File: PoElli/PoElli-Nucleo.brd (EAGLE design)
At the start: 57.5 x 70 mm, 107 parts, among them J3 M022.54MM, J4 M022.54MM, Q3 FDMC2674HANDSOLDERING, Q4 FDMC2674HANDSOLDERING, T1 Coilcraft 230NL, T2 FLYBACK-3_OUTPUTS_749119350, U4 LT3748, U5 TPS2378, U6 ENC424J600, X1 POE-TP-SHIELDED-LEDSTE1888250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

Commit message: Fix SPI pin order
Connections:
- net ETH_MOSI: now also U$2.CN10_29; no longer U$2.CN10_25
- net ETH_SCK: now also U$2.CN10_31; no longer U$2.CN10_29
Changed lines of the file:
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@@
 <contactref element="U6" pad="37"/>
 <contactref element="TP3" pad="P$1"/>
-<contactref element="U$2" pad="CN10_29"/>
-<wire x1="56.7" y1="76.59" x2="96.36" y2="84.02" width="0" layer="19" extent="1-1"/>
+<contactref element="U$2" pad="CN10_31"/>
+<wire x1="56.7" y1="76.59" x2="98.9" y2="84.02" width="0" layer="19" extent="1-1"/>
 <wire x1="24.13" y1="62.8" x2="56.7" y2="76.59" width="0" layer="19" extent="1-1"/>
 </signal>
@@
 <contactref element="U6" pad="36"/>
 <contactref element="TP4" pad="P$1"/>
-<contactref element="U$2" pad="CN10_25"/>
-<wire x1="56.7" y1="77.39" x2="91.28" y2="84.02" width="0" layer="19" extent="1-1"/>
+<contactref element="U$2" pad="CN10_29"/>
+<wire x1="56.7" y1="77.39" x2="96.36" y2="84.02" width="0" layer="19" extent="1-1"/>
 <wire x1="32.55" y1="58.3" x2="56.7" y2="77.39" width="0" layer="19" extent="1-1"/>
 </signal>

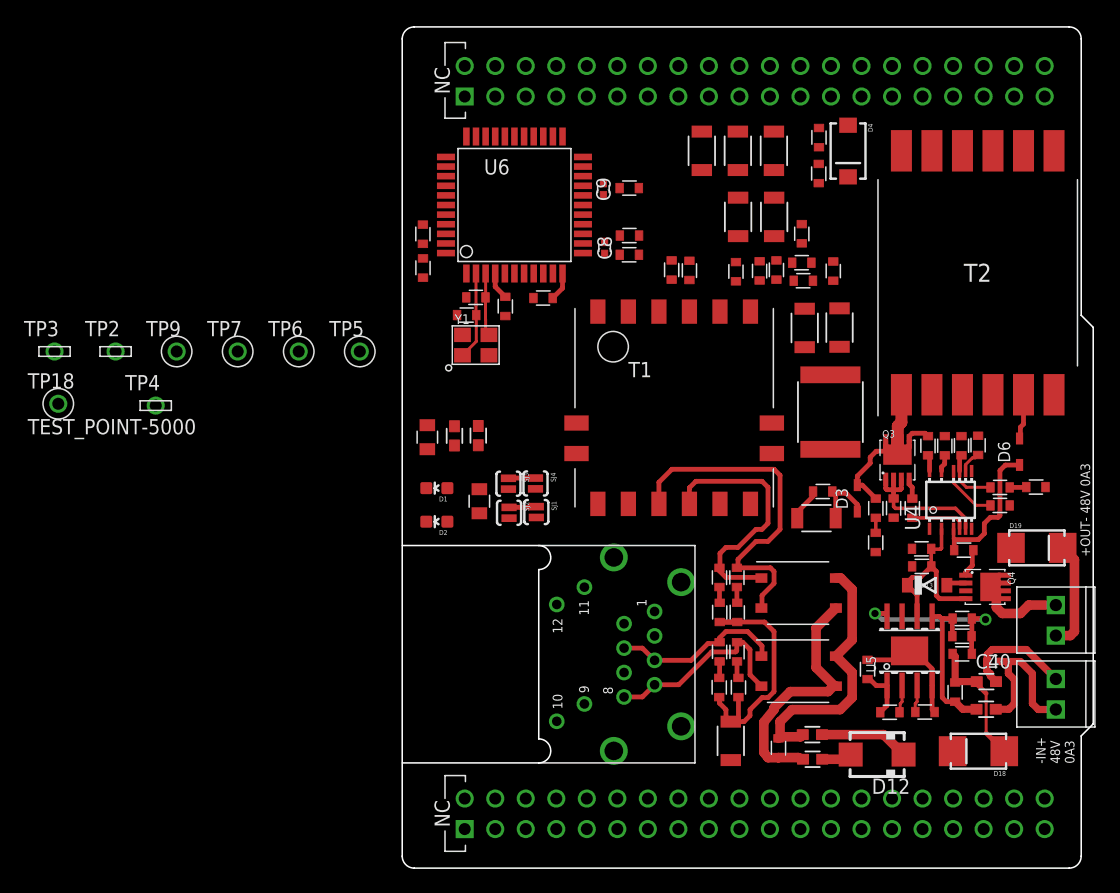
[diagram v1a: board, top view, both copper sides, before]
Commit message: Component placement complete
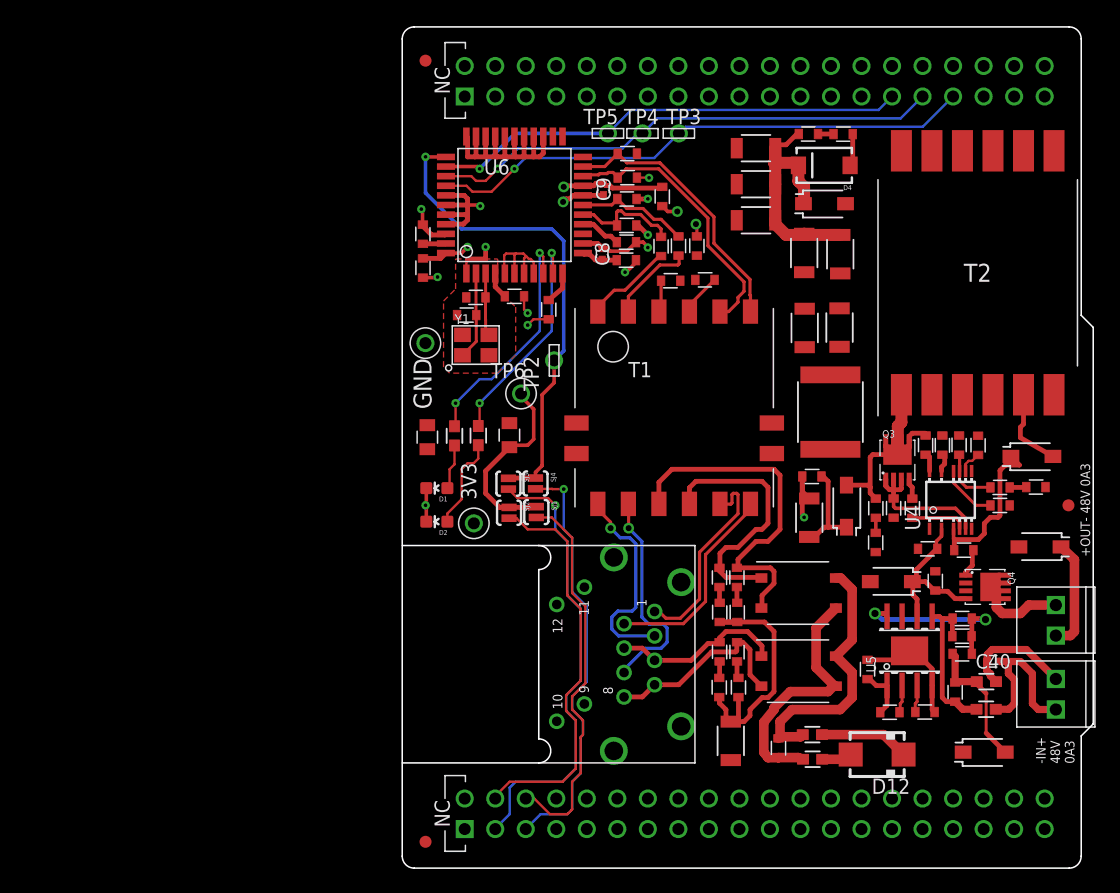
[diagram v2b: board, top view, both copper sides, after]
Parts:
- removed TP18: TEST_POINT-5000, ELL-i-Passives:TP_5000
- removed TP7: (no value), ELL-i-Passives:TP_5000
- added 3V3: (no value), ELL-i-Passives:TP_5000
- added D10: MMSZ4694, ELL-i-DIscreteSemi:SOD-123FL-A
- added FID1, FID2, FID3: FIDUCIAL1X2, SparkFun-Aesthetics:FIDUCIAL-1X2
- D13: value 18V -> MMSZ4694 (8V2); device ELL-i-DIscreteSemi:SOD-123FL -> ELL-i-DIscreteSemi:SOD-123FL-A
- D18, D19: value B2100 -> SMD1200PL; device ELL-i-DIscreteSemi:DIODE-B2100 -> ELL-i-DIscreteSemi:SOD-123FL-A
- D3: value BAV20WS -> SMD1200PL; device ELL-i-DIscreteSemi:SOD-323 -> ELL-i-DIscreteSemi:SOD-123FL-A
- D6: value BAS70J -> SMD1200PL; device ELL-i-DIscreteSemi:SOD-323 -> ELL-i-DIscreteSemi:SOD-123FL-A
- TP5: value (none) -> TEST_POINT-5021; device ELL-i-Passives:TP_5000 -> ELL-i-Passives:TP_5021
- moved TP3 55.0 mm to (76.1, 81.0)
- moved TP4 46.4 mm to (73.0, 81.0)
- moved TP2 36.5 mm to (65.7, 62.1), turned to 90 degrees
- moved TP5 27.5 mm to (70.2, 81.0)
- moved TP9 20.7 mm to (55.0, 63.5)
- moved TP6 18.8 mm to (63.0, 59.3)
- moved R13 18.8 mm to (71.8, 77.3), turned to 0 degrees
- moved R8 15.5 mm to (71.8, 75.5)
- moved R9 15.4 mm to (71.7, 73.3)
- moved R12 13.4 mm to (71.8, 79.3), turned to 0 degrees
- moved C12 11.6 mm to (75.4, 68.7), turned to 180 degrees
- moved C15 8.45 mm to (74.6, 71.5), turned to 90 degrees
- moved C11 8.39 mm to (76.0, 71.6)
- moved C46 6.31 mm to (89.5, 70.9)
- moved C47 6.26 mm to (86.5, 71.0)
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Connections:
- removed net N$36: D1.A, R4.P$2
- removed net N$38: D2.A, R3.P$1
- new net LEDA: D2.A, R3.P$1, X1.10
- new net LEDB: D1.A, R4.P$2, X1.11
- net +3V3: now also 3V3.P$1; no longer TP7.P$1
- net GNDA: now also D10.A, X1.12, X1.9
- net SGND: no longer TP18.P$1
- net VIN: now also D10.C
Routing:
- net GNDA: track 0.00 -> 76.4 mm, vias 0 -> 10
- net ETH_SCK: track 0.00 -> 45.7 mm, vias 0 -> 1
- net ETH_MOSI: track 0.00 -> 42.7 mm, vias 0 -> 1
- net ETH_MISO: track 0.00 -> 39.7 mm, vias 0 -> 1
- net ETH_SS: track 2.27 -> 40.8 mm, vias 0 -> 1
- net N$11: track 0.00 -> 38.2 mm, vias 0 -> 1
- net N$12: track 0.00 -> 35.6 mm, vias 0 -> 1
- net N$13: track 0.00 -> 33.7 mm
- net N$14: track 0.00 -> 32.5 mm
- net TPOUT+: track 0.00 -> 23.0 mm
- net TPOUT-: track 0.00 -> 22.7 mm
- net VIN: track 0.00 -> 21.4 mm
- net N$41: track 0.00 -> 19.8 mm, vias 0 -> 2
- net N$42: track 0.00 -> 18.7 mm, vias 0 -> 2
- net RX-: track 0.00 -> 18.3 mm, vias 0 -> 1
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- added copper zone on layer 15, net ENC-3V3
- added copper zone on layer 1, net GNDA
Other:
- board text added: "GND"

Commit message: component placement, planes final.
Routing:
- net +3V3: track 2.41 -> 113.2 mm, vias 2 -> 5
- net GNDA: track 76.4 -> 129.4 mm, vias 10 -> 27
- net RTN: track 15.4 -> 60.8 mm, vias 0 -> 17
- net N$11: track 38.2 -> 0.00 mm, vias 1 -> 0
- net VDD: track 17.4 -> 54.5 mm, vias 1 -> 12
- net N$12: track 35.6 -> 0.00 mm, vias 1 -> 0
- net N$13: track 33.7 -> 0.00 mm
- net N$14: track 32.5 -> 0.00 mm
- net ETH_INT: track 16.0 -> 44.9 mm, vias 0 -> 2
- net SGND: track 0.00 -> 24.9 mm
- net TRAFO_OUT: track 2.69 -> 25.4 mm
- net ENC-3V3: track 18.7 -> 40.0 mm, vias 3 -> 8
- net TPINCT: track 5.12 -> 16.1 mm
- net VIN: track 21.4 -> 32.0 mm, vias 0 -> 2
- net VSS: track 12.5 -> 7.65 mm, vias 0 -> 3
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- added copper zone on layer 2, net GNDA
- added copper zone on layer 2, net RTN
- added copper zone on layer 15, net VDD
- added copper zone on layer 15, net VIN
- added copper zone on layer 1, net VSS
- added copper zone on layer 2, net VSS

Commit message: Layout complete, except silkscreen.
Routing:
- net N$11: track 0.00 -> 36.6 mm
- net N$13: track 0.00 -> 33.2 mm, vias 0 -> 1
- net N$12: track 0.00 -> 33.0 mm, vias 0 -> 1
- net N$14: track 0.00 -> 30.5 mm, vias 0 -> 1
- net LEDA: track 7.43 -> 32.6 mm
- net LEDB: track 3.80 -> 23.8 mm, vias 0 -> 1
- net RTN: vias 17 -> 18
- added copper zone on layer 15, net RTN

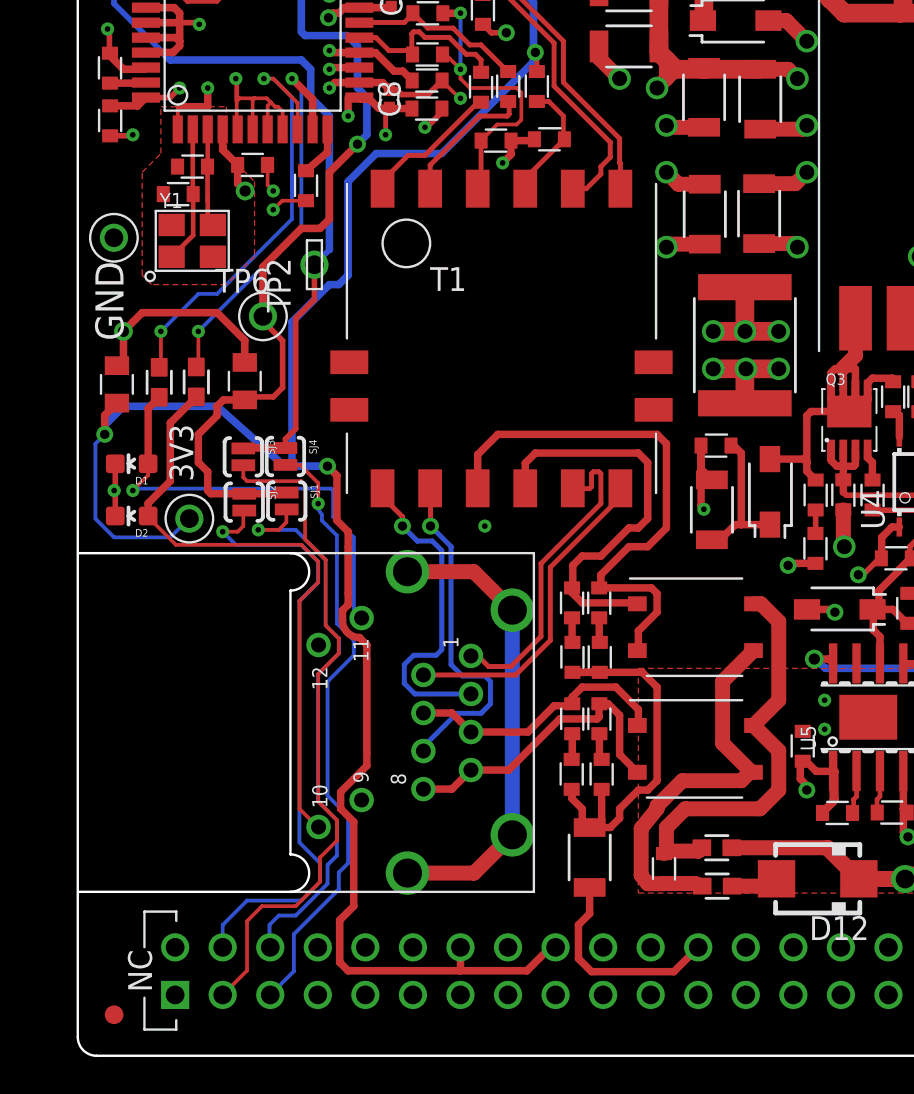
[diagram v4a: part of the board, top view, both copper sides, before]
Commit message: Copper layers, complete, DRC ok. Silkscreen has to be adjusted.
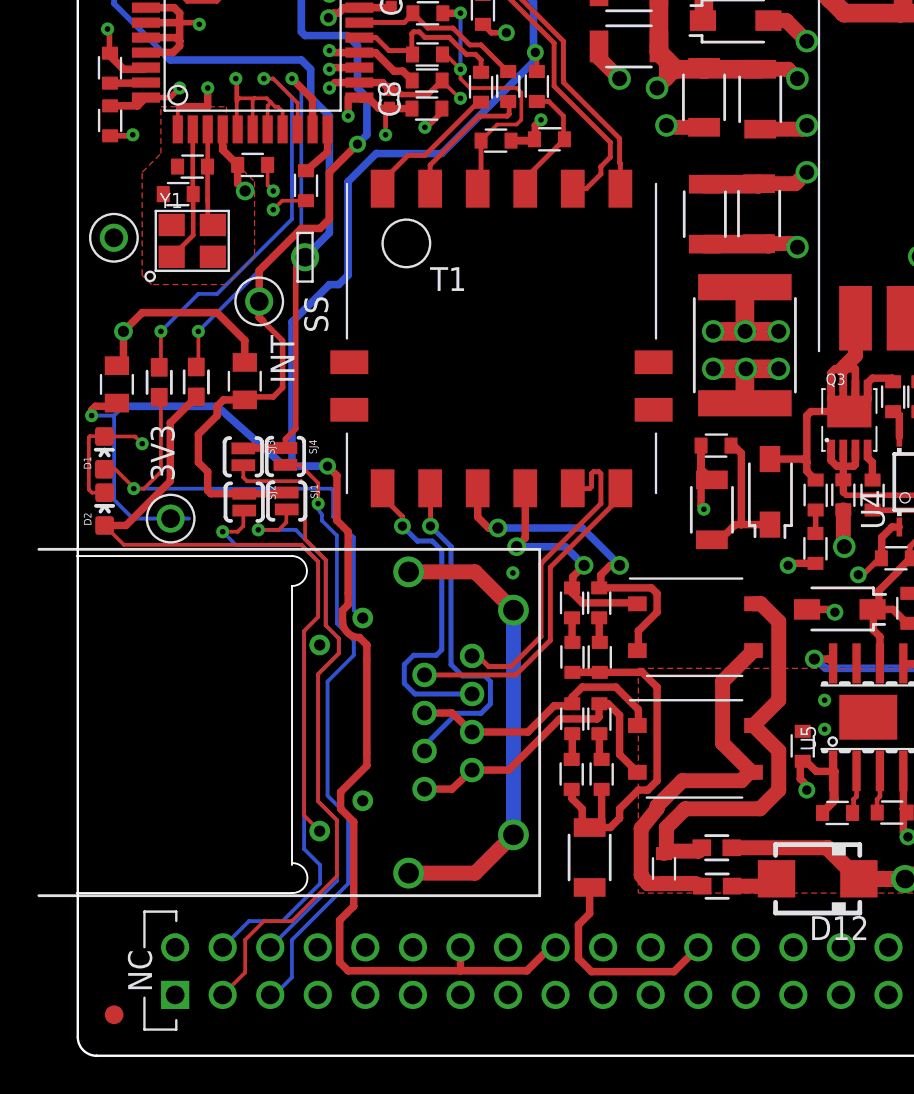
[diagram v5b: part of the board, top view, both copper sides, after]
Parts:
- removed TP2: (no value), ELL-i-Passives:TP_5021
- removed TP6: (no value), ELL-i-Passives:TP_5000
- added INT: (no value), ELL-i-Passives:TP_5000
- added SS: (no value), ELL-i-Passives:TP_5021
- X1: value POE-TP-SHIELDED-LEDSTE1888250 -> POE-TP-SHIELDED-LEDSTE1888250-A; device ELL-i-Connectors:TE1888250 -> ELL-i-Connectors:TE1888250-A
- moved X1 11.4 mm to (64.5, 37.6)
- moved D1 1.57 mm to (54.5, 52.0), turned to 0 degrees
- moved D2 1.50 mm to (54.5, 49.0), turned to 0 degrees
- moved 3V3 1.00 mm to (58.0, 48.5)
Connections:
- net ETH_INT: now also INT.P$1; no longer TP6.P$1
- net ETH_SS: now also SS.P$1; no longer TP2.P$1
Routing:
- net POE_A-: track 29.0 -> 18.8 mm, vias 0 -> 2
- net POE_A+: track 21.6 -> 12.8 mm, vias 0 -> 2
- net GNDA: track 129.4 -> 134.9 mm, vias 27 -> 26
- net LEDA: track 32.6 -> 37.1 mm
- net LEDB: track 23.8 -> 26.1 mm
- net RTN: track 60.8 -> 62.2 mm, vias 18 -> 17
- net +3V3: track 113.2 -> 111.9 mm
- net N$13: track 33.2 -> 32.3 mm
- net SGND: track 24.9 -> 25.4 mm
- net N$14: track 30.5 -> 30.0 mm
- added copper zone on layer 2, net N$1
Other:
- board text removed: "GND"

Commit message: Silkscreen ok
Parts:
- removed TP5: TEST_POINT-5021, ELL-i-Passives:TP_5021
- added MISO: MISO, ELL-i-Passives:TP_5021
- 3V3: value (none) -> 3V3
- C40: device ELL-i-Passives:SMD0402-B -> ELL-i-Passives:SMD0603-B
- D1: value GREEN -> LINK
- D2: value GREEN -> ACT
- INT: value (none) -> TEST_POINT-5000
- SS: value (none) -> SS
- TP3: value (none) -> SCK
- TP4: value (none) -> MOSI
- TP9: value (none) -> GND
- moved TP3 1.80 mm to (77.9, 81.0)
- moved TP4 1.80 mm to (74.8, 81.0)
- moved C40 0.79 mm to (102.5, 37.8), turned to 270 degrees
- moved C33 0.46 mm to (92.0, 49.7)
- moved Q3 0.40 mm to (93.9, 53.8)
- moved R22 0.35 mm to (96.8, 46.0)
- moved U4 0.30 mm to (98.7, 50.1)
- moved C30 0.25 mm to (99.8, 46.0)
- moved C35 0.20 mm to (91.6, 36.3)
- moved D13 0.10 mm to (93.8, 43.8)
- moved R23 0.10 mm to (93.6, 32.7)
- moved R26 0.10 mm to (97.4, 43.8)
- moved R28 0.10 mm to (95.5, 49.7)
- moved R32 0.10 mm to (94.0, 49.7)
- moved R27 0.10 mm to (92.5, 46.8)
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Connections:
- net ETH_MISO: now also MISO.P$1; no longer TP5.P$1
- net N$53: now also C40.P$1; no longer C40.1
- net N$55: now also C40.P$2; no longer C40.2
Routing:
- net RTN: track 62.2 -> 60.3 mm
- net N$28: track 21.3 -> 22.9 mm, vias 0 -> 4
- net N$10: track 15.9 -> 17.5 mm, vias 0 -> 4
- net N$53: track 9.52 -> 10.5 mm
- net +3V3: track 111.9 -> 110.9 mm
- net VSS: track 7.65 -> 7.73 mm, vias 3 -> 9
- added copper zone on layer 16, net N$10
- added copper zone on layer 16, net N$28
- added copper zone on layer 16, net VSS
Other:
- board text added: "AC"
- board text added: "DC"

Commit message: PoELLi 1.0
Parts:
- added LOGO1: OSHW-LOGOM, SparkFun-Aesthetics:OSHW-LOGO-M
- SJ1, SJ3: value SOLDERJUMPERNO -> SOLDERJUMPERNC2; device SparkFun-Passives:SJ_2S-NO -> SparkFun-Passives:SJ_2S-NOTRACE
- moved TP3 9.15 mm to (68.7, 81.0)
- moved MISO 6.50 mm to (75.2, 81.0)
- moved TP4 3.50 mm to (78.3, 81.0)
- moved D19 1.41 mm to (105.1, 47.6)
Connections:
- removed net N$10: J3.P2, Q4.5, Q4.6, Q4.7, Q4.8, Q4.F1
- removed net N$21: D19.C, J3.P1
- new net N$3: J3.P1, Q4.5, Q4.6, Q4.7, Q4.8, Q4.F1
- new net N$4: D19.C, J3.P2
- net ETH_MISO: now also U$2.CN10_13; no longer U$2.CN10_27
- net ETH_MOSI: now also U$2.CN10_15; no longer U$2.CN10_29
- net ETH_SCK: now also U$2.CN10_11; no longer U$2.CN10_31
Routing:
- net ETH_SCK: track 45.7 -> 20.5 mm
- net N$3: track 0.00 -> 19.6 mm, vias 0 -> 4
- net N$10: track 17.5 -> 0.00 mm, vias 4 -> 0
- net ETH_MISO: track 39.7 -> 25.0 mm
- net ETH_MOSI: track 42.8 -> 28.3 mm
- net N$21: track 9.25 -> 0.00 mm
- net N$4: track 0.00 -> 6.13 mm
- net VDD: track 54.4 -> 51.4 mm, vias 12 -> 11
- net VSS: track 7.73 -> 9.95 mm, vias 9 -> 10
- net GNDA: track 134.9 -> 133.8 mm, vias 26 -> 27
- added copper zone on layer 16, net N$3
- removed copper zone on layer 16, net N$10
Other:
- board text added: "48V 0A3 -IN+"
- board text added: "48V 0A3 -OUT+"
- board text added: "ELL-i"
- board text added: "OPEN HARDWARE"
- board text added: "Open source co-operative"
- board text added: "PoELLi-Nucleo 1.0"
- board text added: "QC pass"
- board text added: "http://ell-i.org/"
- board text added: "https://github.com/Ell-i /ELL-i-Eagle-Boards"
- board text removed: "+OUT- 48V 0A3"
- board text removed: "-IN+ 48V 0A3"

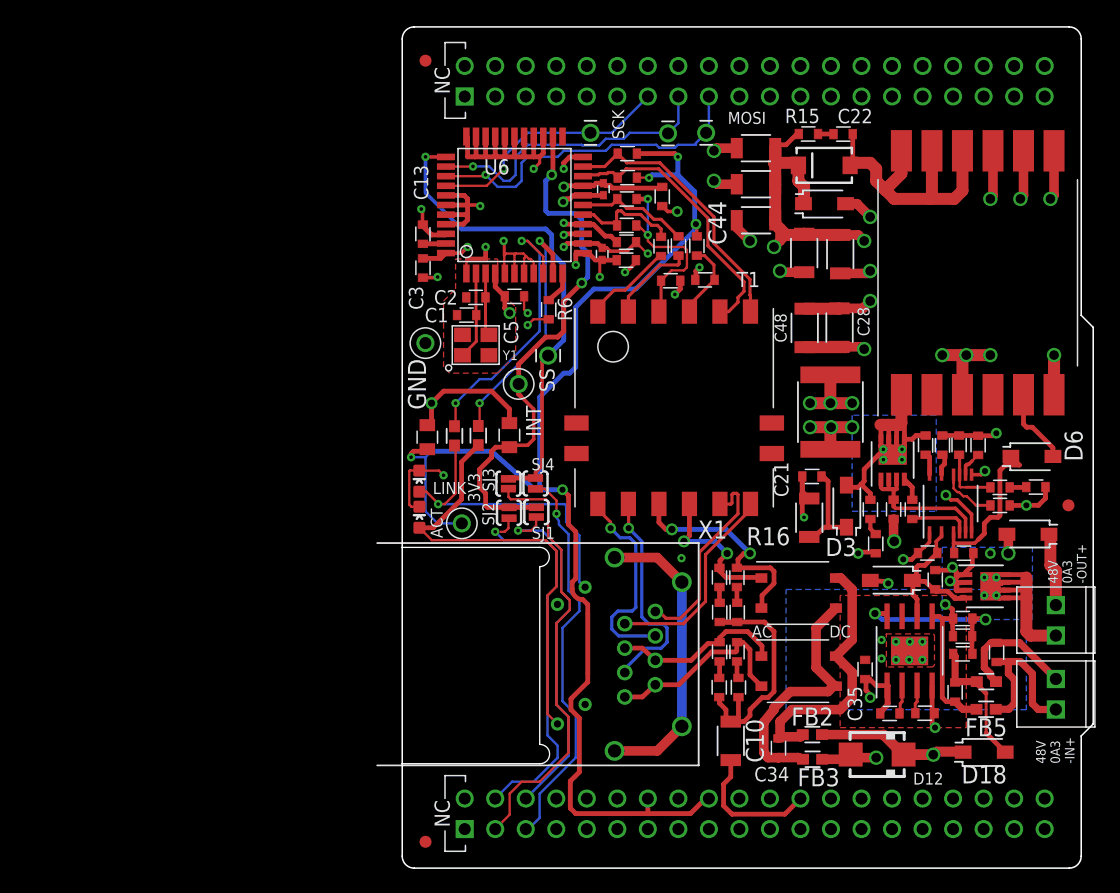
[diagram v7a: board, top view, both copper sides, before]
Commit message: Fix Bridge rectifier connection
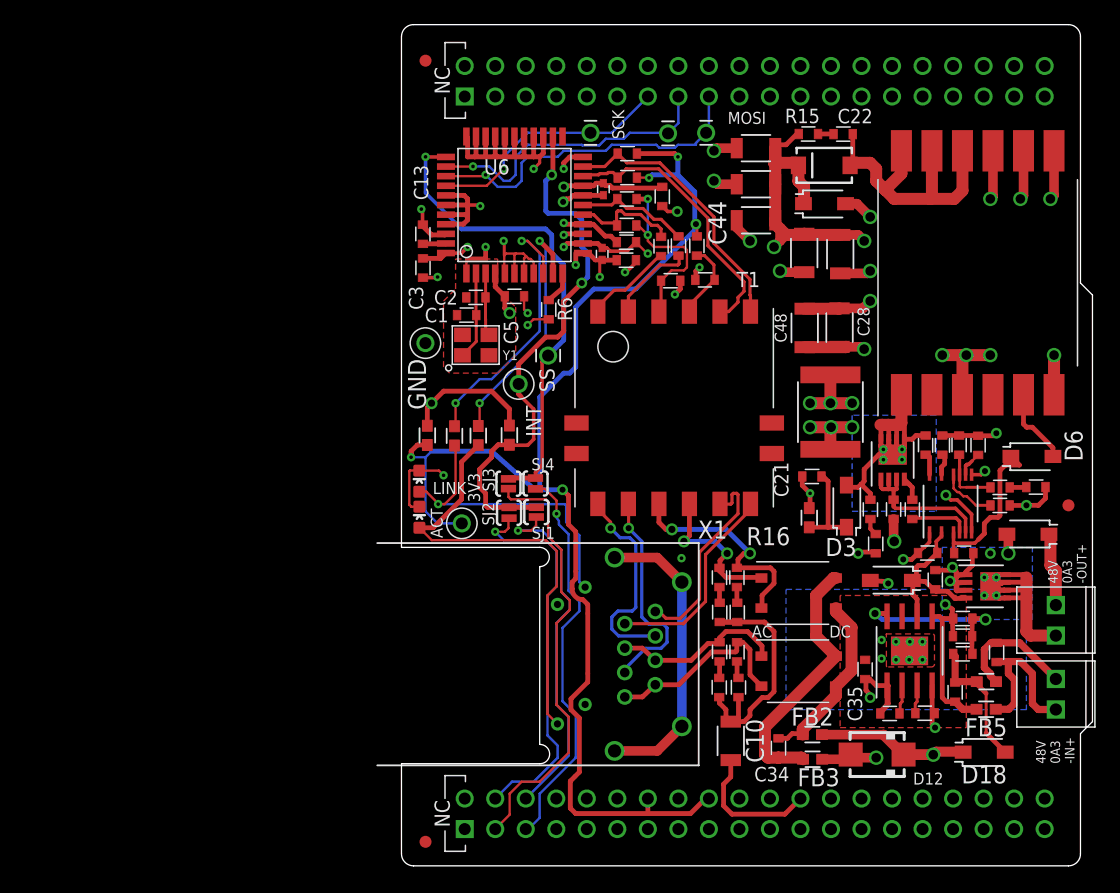
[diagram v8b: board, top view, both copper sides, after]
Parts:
- C22: value 470pF -> 150p
- C39: value 470p -> 150p
- FB1: device ELL-i-Passives:SMD0805-A -> ELL-i-Passives:SMD0603-A
- R14: value 100k -> 270k; device ELL-i-Passives:SMD0805-A -> ELL-i-Passives:SMD0603-A
- R15: value 10R -> 220R
- R16: value 2k -> 270k; device ELL-i-Passives:SMD1206-A -> ELL-i-Passives:SMD0603-A
- R22: value 357k -> 24k9
- R24: value TBD -> 270k
- R26: value 16k5 -> 6k04
- R28: value 0R -> 10R
- R31: value 28k -> 24k9
- R32: value 0R10 -> 0R082
- R33: value 12k -> 12k4
- R35: value 237k -> 270k
- R36: value 10k -> 12k4
- moved FB1 0.15 mm to (55.1, 55.8)
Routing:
- net N$6: track 22.1 -> 15.0 mm
- net VDD: track 51.4 -> 48.7 mm
- net N$8: track 21.3 -> 22.0 mm
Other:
- outline, holes or cut-outs redrawn
